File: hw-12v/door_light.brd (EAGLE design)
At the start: 26.2 x 28.6 mm, 24 parts, among them IC1 TINY13-20SSU, IC2 78L05F, T1 IRFML8244, T2 IRFML8244, T3 KP-3216P3C

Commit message: recalculated some resitors values
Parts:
- R2: value 470R -> 180R
- R7, R9: value 2.9kR -> 2.7kR
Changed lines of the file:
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@@
 <layer number="19" name="Unrouted" color="6" fill="1" visible="yes" active="yes"/>
 <layer number="20" name="Dimension" color="15" fill="1" visible="yes" active="yes"/>
-<layer number="21" name="tPlace" color="7" fill="1" visible="no" active="yes"/>
-<layer number="22" name="bPlace" color="7" fill="1" visible="no" active="yes"/>
-<layer number="23" name="tOrigins" color="15" fill="1" visible="no" active="yes"/>
-<layer number="24" name="bOrigins" color="15" fill="1" visible="no" active="yes"/>
+<layer number="21" name="tPlace" color="7" fill="1" visible="yes" active="yes"/>
+<layer number="22" name="bPlace" color="7" fill="1" visible="yes" active="yes"/>
+<layer number="23" name="tOrigins" color="15" fill="1" visible="yes" active="yes"/>
+<layer number="24" name="bOrigins" color="15" fill="1" visible="yes" active="yes"/>
 <layer number="25" name="tNames" color="7" fill="1" visible="no" active="yes"/>
 <layer number="26" name="bNames" color="7" fill="1" visible="no" active="yes"/>
@@
 <layer number="45" name="Holes" color="7" fill="1" visible="no" active="yes"/>
 <layer number="46" name="Milling" color="3" fill="1" visible="no" active="yes"/>
-<layer number="47" name="Measures" color="7" fill="1" visible="no" active="yes"/>
-<layer number="48" name="Document" color="7" fill="1" visible="no" active="yes"/>
-<layer number="49" name="Reference" color="7" fill="1" visible="no" active="yes"/>
-<layer number="51" name="tDocu" color="7" fill="1" visible="no" active="yes"/>
-<layer number="52" name="bDocu" color="7" fill="1" visible="no" active="yes"/>
+<layer number="47" name="Measures" color="7" fill="1" visible="yes" active="yes"/>
+<layer number="48" name="Document" color="7" fill="1" visible="yes" active="yes"/>
+<layer number="49" name="Reference" color="7" fill="1" visible="yes" active="yes"/>
+<layer number="51" name="tDocu" color="7" fill="1" visible="yes" active="yes"/>
+<layer number="52" name="bDocu" color="7" fill="1" visible="yes" active="yes"/>
 <layer number="91" name="Nets" color="2" fill="1" visible="no" active="no"/>
 <layer number="92" name="Busses" color="1" fill="1" visible="no" active="no"/>
@@
 <element name="F1" library="rcl" package="MINI_MELF-0204W" value="F750mA" x="47.41" y="50.47" rot="R90"/>
 <element name="R5" library="rcl" package="R0402" value="10kR" x="28.5" y="56"/>
-<element name="R7" library="rcl" package="R0603" value="2.9kR" x="33" y="45" rot="R180"/>
+<element name="R7" library="rcl" package="R0603" value="2.7kR" x="33" y="45" rot="R180"/>
 <element name="R8" library="rcl" package="R0603" value="10kR" x="26" y="56" rot="R90"/>
 <element name="R6" library="rcl" package="R0603" value="10kR" x="33" y="47"/>
-<element name="R9" library="rcl" package="R0603" value="2.9kR" x="26" y="47" rot="R90"/>
+<element name="R9" library="rcl" package="R0603" value="2.7kR" x="26" y="47" rot="R90"/>
 <element name="LED2" library="led" package="CHIPLED_1206" value="IR" x="42.28" y="45.55"/>
 <element name="LED1" library="led" package="CHIPLED_0603" value="RED" x="40" y="45"/>
-<element name="R2" library="rcl" package="R0603" value="470R" x="43" y="51" rot="R270"/>
+<element name="R2" library="rcl" package="R0603" value="180R" x="43" y="51" rot="R270"/>
 <element name="R1" library="rcl" package="R0603" value="470R" x="41" y="51" rot="R270"/>
 <element name="T3" library="opto-trans-smd" package="OPTO-TRANS-SIEMENS_BP103" value="KP-3216P3C" x="28.82" y="45.67" rot="R270">

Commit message: elements are now more compact
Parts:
- moved T3 3.68 mm to (32.5, 45.5), turned to 180 degrees
- moved R7 3.20 mm to (30.5, 47.0), turned to 0 degrees
- moved LED1 3.16 mm to (41.0, 48.0)
- moved LED2 2.83 mm to (39.5, 45.0), turned to 270 degrees
- moved R6 1.50 mm to (34.5, 47.0)
- moved SJ2 1.00 mm to (47.0, 45.0)
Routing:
- net N$1: track 4.81 -> 1.40 mm
- net N$2: track 3.15 -> 6.51 mm
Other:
- board size 26.2 x 28.6 mm -> 26.2 x 27.6 mm
- board text added: "v2.0.0 (rc7)"
- board text removed: "v2.0.0 (rc6)"
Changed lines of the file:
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@@
 <board>
 <plain>
-<wire x1="22.78" y1="40.75" x2="49" y2="40.75" width="0" layer="20"/>
-<wire x1="49" y1="40.75" x2="49" y2="69.38" width="0" layer="20"/>
+<wire x1="22.78" y1="41.75" x2="49" y2="41.75" width="0" layer="20"/>
+<wire x1="49" y1="41.75" x2="49" y2="69.38" width="0" layer="20"/>
 <wire x1="49" y1="69.38" x2="22.78" y2="69.38" width="0" layer="20"/>
-<wire x1="22.78" y1="69.38" x2="22.78" y2="40.75" width="0" layer="20"/>
-<text x="48.8" y="46.6" size="1.27" layer="1" rot="R90">+</text>
+<wire x1="22.78" y1="69.38" x2="22.78" y2="41.75" width="0" layer="20"/>
+<text x="48.8" y="47" size="1.27" layer="1" rot="R90">+</text>
 <text x="48.7" y="65.5" size="1.27" layer="1" rot="R90">LED</text>
 <text x="25.5" y="64.6" size="1.27" layer="1">v2.0.0
-(rc6)</text>
+(rc7)</text>
 </plain>
 <attributes>
@@
 <element name="F1" library="rcl" package="MINI_MELF-0204W" value="F750mA" x="47.41" y="50.47" rot="R90"/>
 <element name="R5" library="rcl" package="R0402" value="10kR" x="28.5" y="56"/>
-<element name="R7" library="rcl" package="R0603" value="2.7kR" x="33" y="45" rot="R180"/>
+<element name="R7" library="rcl" package="R0603" value="2.7kR" x="30.5" y="47"/>
 <element name="R8" library="rcl" package="R0603" value="10kR" x="26" y="56" rot="R90"/>
-<element name="R6" library="rcl" package="R0603" value="10kR" x="33" y="47"/>
+<element name="R6" library="rcl" package="R0603" value="10kR" x="34.5" y="47"/>
 <element name="R9" library="rcl" package="R0603" value="2.7kR" x="26" y="47" rot="R90"/>
-<element name="LED2" library="led" package="CHIPLED_1206" value="IR" x="42.28" y="45.55"/>
-<element name="LED1" library="led" package="CHIPLED_0603" value="RED" x="40" y="45"/>
+<element name="LED2" library="led" package="CHIPLED_1206" value="IR" x="39.5" y="45" rot="R270"/>
+<element name="LED1" library="led" package="CHIPLED_0603" value="RED" x="41" y="48"/>
 <element name="R2" library="rcl" package="R0603" value="180R" x="43" y="51" rot="R270"/>
 <element name="R1" library="rcl" package="R0603" value="470R" x="41" y="51" rot="R270"/>
-<element name="T3" library="opto-trans-smd" package="OPTO-TRANS-SIEMENS_BP103" value="KP-3216P3C" x="28.82" y="45.67" rot="R270">
-<attribute name="OC_NEWARK" value="unknown" x="28.82" y="45.67" size="1.778" layer="27" rot="R270" display="off"/>
-<attribute name="MPN" value="" x="28.82" y="45.67" size="1.778" layer="27" rot="R270" display="off"/>
-<attribute name="MF" value="" x="28.82" y="45.67" size="1.778" layer="27" rot="R270" display="off"/>
-<attribute name="OC_FARNELL" value="unknown" x="28.82" y="45.67" size="1.778" layer="27" rot="R270" display="off"/>
+<element name="T3" library="opto-trans-smd" package="OPTO-TRANS-SIEMENS_BP103" value="KP-3216P3C" x="32.5" y="45.5" rot="R180">
+<attribute name="OC_NEWARK" value="unknown" x="32.5" y="45.5" size="1.778" layer="27" rot="R180" display="off"/>
+<attribute name="MPN" value="" x="32.5" y="45.5" size="1.778" layer="27" rot="R180" display="off"/>
+<attribute name="MF" value="" x="32.5" y="45.5" size="1.778" layer="27" rot="R180" display="off"/>
+<attribute name="OC_FARNELL" value="unknown" x="32.5" y="45.5" size="1.778" layer="27" rot="R180" display="off"/>
 </element>
 <element name="T1" library="zetex" package="SOT-23" value="IRFML8244" x="38" y="51" rot="R180">
@@
 <attribute name="OC_FARNELL" value="unknown" x="38" y="51" size="1.778" layer="27" rot="R180" display="off"/>
 </element>
-<element name="SJ2" library="jumper" package="SJW" value="PWR" x="47" y="44" rot="R90"/>
+<element name="SJ2" library="jumper" package="SJW" value="PWR" x="47" y="45" rot="R90"/>
 <element name="SJ1" library="jumper" package="SJW" value="LIGHT" x="47.5" y="63.4" rot="R270"/>
 <element name="R4" library="rcl" package="R0603" value="100kR" x="32" y="63" rot="R180"/>
@@
 <contactref element="C1" pad="2"/>
 <polygon width="0.6096" layer="1" isolate="0.6096" orphans="yes">
-<vertex x="23.05" y="41.02"/>
+<vertex x="23.05" y="42.02"/>
 <vertex x="23.05" y="69.12"/>
 <vertex x="49.5" y="69.12"/>
-<vertex x="49.5" y="41.02"/>
+<vertex x="49.5" y="42.02"/>
 </polygon>
 <contactref element="R7" pad="1"/>
@@
 <contactref element="LED2" pad="C"/>
 <contactref element="R2" pad="2"/>
-<wire x1="43" y1="50.15" x2="43" y2="48.02" width="0.4064" layer="1"/>
-<wire x1="43" y1="48.02" x2="42.28" y2="47.3" width="0.4064" layer="1"/>
+<wire x1="41.25" y1="45" x2="41.72" y2="44.72" width="0.4064" layer="1"/>
+<wire x1="41.72" y1="44.72" x2="43" y2="46" width="0.4064" layer="1"/>
+<wire x1="43" y1="46" x2="43" y2="50.15" width="0.4064" layer="1"/>
 </signal>
 <signal name="N$4">
@@
 <contactref element="SJ2" pad="2"/>
 <wire x1="47.41" y1="48.97" x2="47.41" y2="45.68" width="0.8128" layer="1"/>
-<wire x1="47.41" y1="45.68" x2="47" y2="45.27" width="0.4064" layer="1"/>
+<wire x1="47.41" y1="45.68" x2="47" y2="46.27" width="0.4064" layer="1"/>
 </signal>
 <signal name="N$12">
@@
 <contactref element="IC1" pad="2"/>
 <contactref element="T3" pad="COLLECTOR"/>
-<wire x1="29.29" y1="47.04" x2="29.29" y2="47.29" width="0.4064" layer="1"/>
-<wire x1="29.29" y1="47.29" x2="30" y2="48" width="0.4064" layer="1"/>
-<wire x1="30" y1="48" x2="30" y2="52" width="0.4064" layer="1"/>
-<wire x1="32.15" y1="47" x2="32.15" y2="45" width="0.4064" layer="1"/>
 <wire x1="28.366" y1="52.635" x2="29.365" y2="52.635" width="0.4064" layer="1"/>
 <wire x1="29.365" y1="52.635" x2="30" y2="52" width="0.4064" layer="1"/>
-<wire x1="29.29" y1="47.04" x2="32.11" y2="47.04" width="0.4064" layer="1"/>
-<wire x1="32.11" y1="47.04" x2="32.15" y2="47" width="0.4064" layer="1"/>
+<wire x1="33.61" y1="47.04" x2="33.65" y2="47" width="0.4064" layer="1"/>
+<wire x1="30" y1="52" x2="30" y2="49" width="0.4064" layer="1"/>
+<wire x1="30" y1="49" x2="31.35" y2="47.65" width="0.4064" layer="1"/>
+<wire x1="31.35" y1="47" x2="31.35" y2="47.65" width="0.4064" layer="1"/>
+<wire x1="31.35" y1="47" x2="33.65" y2="47" width="0.4064" layer="1"/>
+<wire x1="33.65" y1="47" x2="33.65" y2="45.1" width="0.4064" layer="1"/>
+<wire x1="33.65" y1="45.1" x2="33.87" y2="45.03" width="0.4064" layer="1"/>
 </signal>
 <signal name="N$17">
@@
 <contactref element="LED1" pad="C"/>
 <contactref element="R1" pad="2"/>
-<wire x1="41" y1="50.15" x2="41" y2="49" width="0.4064" layer="1"/>
-<wire x1="41" y1="49" x2="40" y2="48" width="0.4064" layer="1"/>
-<wire x1="40" y1="48" x2="40" y2="45.75" width="0.4064" layer="1"/>
+<wire x1="41" y1="50.15" x2="41" y2="48.75" width="0.4064" layer="1"/>
 </signal>
 <signal name="N$14">
@@
 <wire x1="43" y1="57" x2="41.8" y2="57" width="0.4064" layer="1"/>
 <wire x1="41.8" y1="57" x2="41" y2="57.8" width="0.4064" layer="1"/>
-<wire x1="42.28" y1="43.8" x2="40.45" y2="43.8" width="0.4064" layer="1"/>
-<wire x1="40.45" y1="43.8" x2="40" y2="44.25" width="0.4064" layer="1"/>
-<wire x1="34" y1="47" x2="33.85" y2="47" width="0.4064" layer="1"/>
-<wire x1="37" y1="44" x2="39.75" y2="44" width="0.4064" layer="1"/>
-<wire x1="39.75" y1="44" x2="40" y2="44.25" width="0.4064" layer="1"/>
-<wire x1="34" y1="47" x2="37" y2="44" width="0.4064" layer="1"/>
-<wire x1="34" y1="47" x2="31" y2="50" width="0.4064" layer="1"/>
 <wire x1="31" y1="50" x2="31" y2="54.15" width="0.4064" layer="1"/>
 <wire x1="26.5" y1="59.5" x2="29.5" y2="59.5" width="0.4064" layer="1"/>
@@
 <wire x1="33.6" y1="58.4" x2="33" y2="59" width="0.4064" layer="1"/>
 <wire x1="33" y1="59" x2="30" y2="59" width="0.4064" layer="1"/>
+<wire x1="31" y1="50" x2="32" y2="49" width="0.4064" layer="1"/>
+<wire x1="32" y1="49" x2="34" y2="49" width="0.4064" layer="1"/>
+<wire x1="34" y1="49" x2="35.35" y2="47.65" width="0.4064" layer="1"/>
+<wire x1="35.35" y1="47" x2="35.35" y2="47.65" width="0.4064" layer="1"/>
+<wire x1="35.35" y1="47" x2="36" y2="47" width="0.4064" layer="1"/>
+<wire x1="36" y1="47" x2="38" y2="45" width="0.4064" layer="1"/>
+<wire x1="38" y1="45" x2="38" y2="44.92" width="0.4064" layer="1"/>
+<wire x1="38" y1="44.92" x2="37.75" y2="45" width="0.4064" layer="1"/>
+<wire x1="38" y1="45" x2="40" y2="47" width="0.4064" layer="1"/>
+<wire x1="40" y1="47" x2="40.75" y2="47" width="0.4064" layer="1"/>
+<wire x1="40.75" y1="47" x2="41" y2="47.25" width="0.4064" layer="1"/>
 </signal>
 <signal name="+12V">

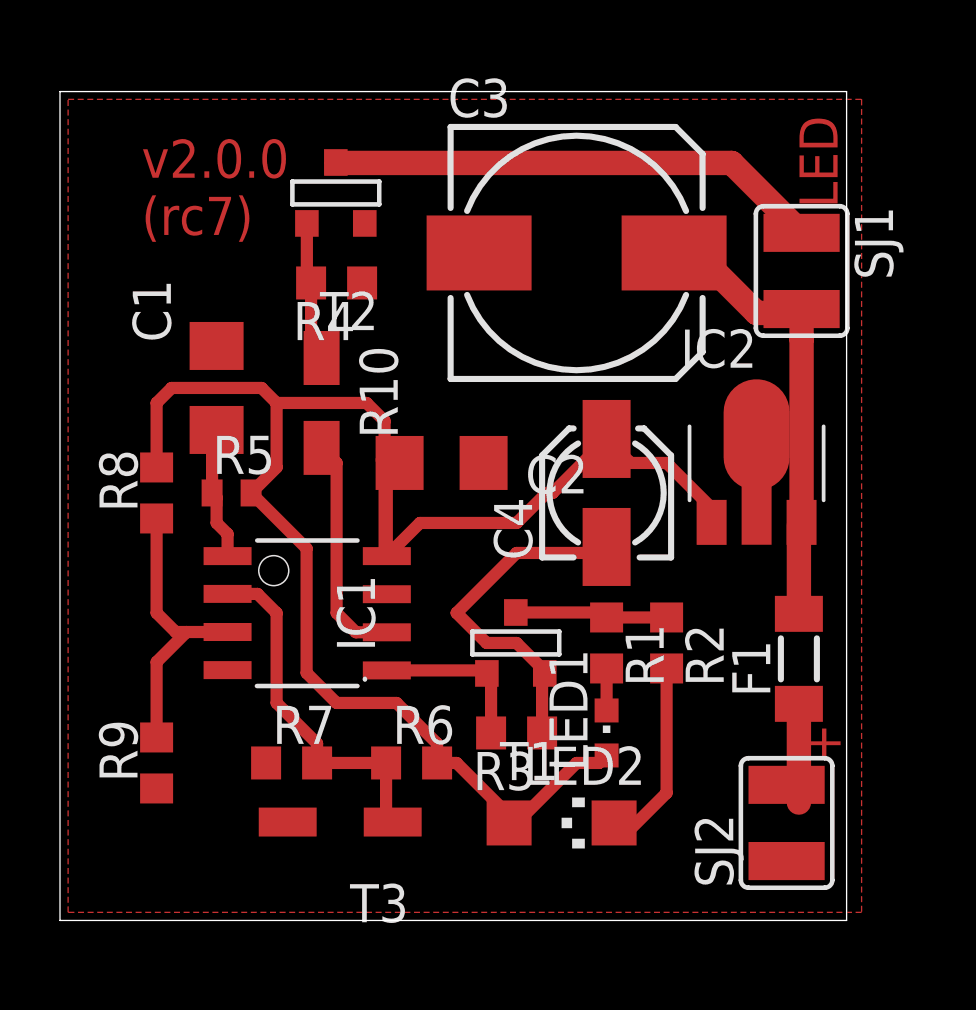
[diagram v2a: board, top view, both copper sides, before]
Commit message: fixed coliding Vcc and GND on board layout
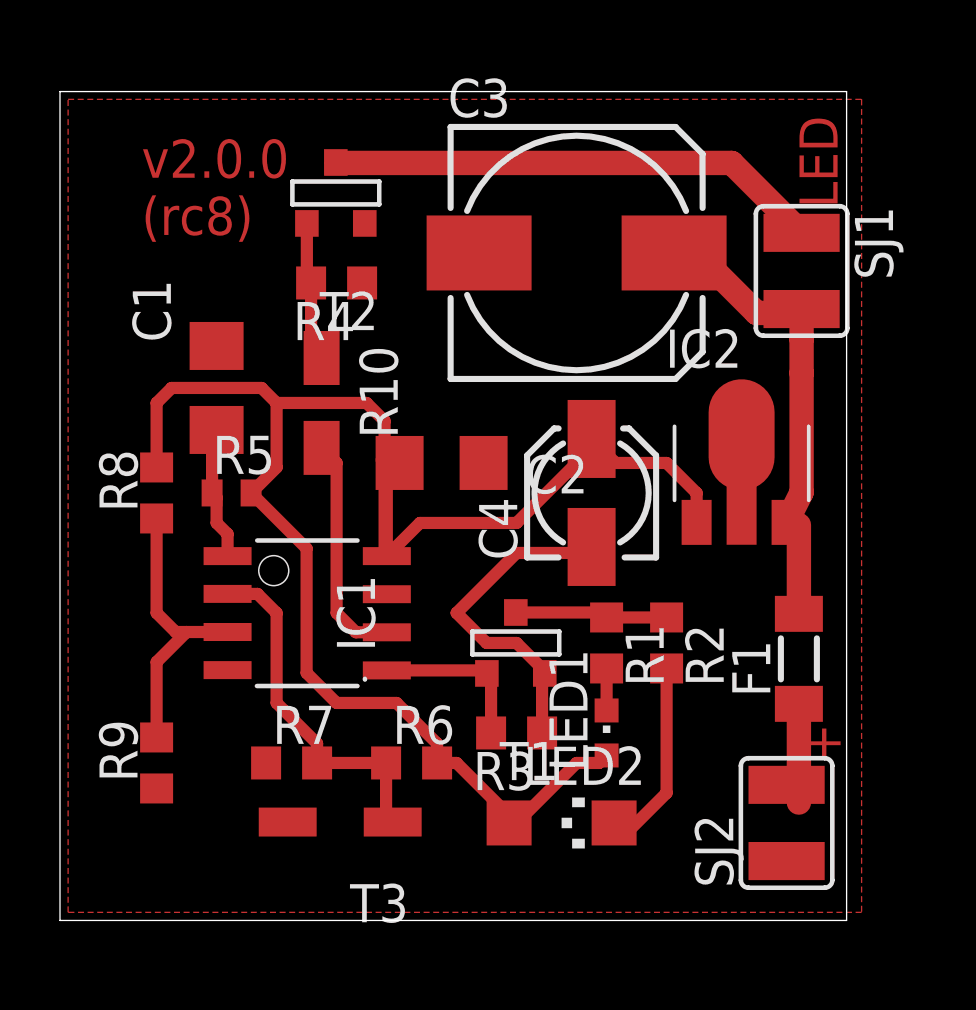
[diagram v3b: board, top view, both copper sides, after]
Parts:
- moved C4 0.50 mm to (40.5, 56.0)
- moved IC2 0.50 mm to (45.5, 57.0)
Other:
- board text added: "v2.0.0 (rc8)"
- board text removed: "v2.0.0 (rc7)"
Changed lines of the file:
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@@
 <text x="48.7" y="65.5" size="1.27" layer="1" rot="R90">LED</text>
 <text x="25.5" y="64.6" size="1.27" layer="1">v2.0.0
-(rc7)</text>
+(rc8)</text>
 </plain>
 <attributes>
@@
 <attribute name="OC_FARNELL" value="unknown" x="32" y="66" size="1.778" layer="27" rot="R180" display="off"/>
 </element>
-<element name="C4" library="rcl" package="153CLV-0405" value="4.7uF" x="41" y="56" rot="R90"/>
+<element name="C4" library="rcl" package="153CLV-0405" value="4.7uF" x="40.5" y="56" rot="R90"/>
 <element name="C3" library="rcl" package="153CLV-0810" value="100uF" x="40" y="64"/>
-<element name="IC2" library="linear" package="SOT89" value="78L05F" x="46" y="57"/>
+<element name="IC2" library="linear" package="SOT89" value="78L05F" x="45.5" y="57"/>
 <element name="R10" library="rcl" package="R1206W" value="0R" x="31.5" y="59" rot="R270"/>
 </elements>
@@
 <wire x1="36" y1="52" x2="38" y2="54" width="0.4064" layer="1"/>
 <wire x1="38" y1="54" x2="40.8" y2="54" width="0.4064" layer="1"/>
-<wire x1="40.8" y1="54" x2="41" y2="54.2" width="0.4064" layer="1"/>
+<wire x1="40.8" y1="54" x2="40.5" y2="54.2" width="0.4064" layer="1"/>
 </signal>
 <signal name="N$2">
@@
 <contactref element="IC2" pad="1"/>
 <contactref element="C4" pad="+"/>
-<wire x1="44.501" y1="55.019" x2="44.501" y2="55.499" width="0.4064" layer="1"/>
-<wire x1="44.501" y1="55.499" x2="43" y2="57" width="0.4064" layer="1"/>
-<wire x1="43" y1="57" x2="41.8" y2="57" width="0.4064" layer="1"/>
-<wire x1="41.8" y1="57" x2="41" y2="57.8" width="0.4064" layer="1"/>
 <wire x1="31" y1="50" x2="31" y2="54.15" width="0.4064" layer="1"/>
 <wire x1="26.5" y1="59.5" x2="29.5" y2="59.5" width="0.4064" layer="1"/>
@@
 <wire x1="34.1" y1="57" x2="33.6" y2="56.4" width="0.4064" layer="1"/>
 <wire x1="34.779" y1="55" x2="38" y2="55" width="0.4064" layer="1"/>
-<wire x1="38" y1="55" x2="39" y2="56" width="0.4064" layer="1"/>
-<wire x1="39" y1="56" x2="39.2" y2="56" width="0.4064" layer="1"/>
 <wire x1="31" y1="54.15" x2="29.15" y2="56" width="0.4064" layer="1"/>
-<wire x1="39.2" y1="56" x2="41" y2="57.8" width="0.4064" layer="1"/>
 <wire x1="33.674" y1="53.895" x2="33.674" y2="56.326" width="0.4064" layer="1"/>
 <wire x1="33.674" y1="56.326" x2="33.6" y2="56.4" width="0.4064" layer="1"/>
@@
 <wire x1="40" y1="47" x2="40.75" y2="47" width="0.4064" layer="1"/>
 <wire x1="40.75" y1="47" x2="41" y2="47.25" width="0.4064" layer="1"/>
+<wire x1="40.5" y1="57.8" x2="40.5" y2="57.5" width="0.4064" layer="1"/>
+<wire x1="40.5" y1="57.5" x2="38" y2="55" width="0.4064" layer="1"/>
+<wire x1="44.001" y1="55.019" x2="44.001" y2="55.999" width="0.4064" layer="1"/>
+<wire x1="44.001" y1="55.999" x2="43" y2="57" width="0.4064" layer="1"/>
+<wire x1="43" y1="57" x2="41.3" y2="57" width="0.4064" layer="1"/>
+<wire x1="41.3" y1="57" x2="40.5" y2="57.8" width="0.4064" layer="1"/>
 </signal>
 <signal name="+12V">
@@
 <contactref element="C3" pad="+"/>
 <wire x1="47.41" y1="51.97" x2="47.41" y2="54.93" width="0.8128" layer="1"/>
-<wire x1="47.41" y1="54.93" x2="47.499" y2="55.019" width="0.4064" layer="1"/>
-<wire x1="47.499" y1="55.019" x2="47.499" y2="61.131" width="0.8128" layer="1"/>
+<wire x1="47.41" y1="54.93" x2="46.999" y2="55.019" width="0.4064" layer="1"/>
+<wire x1="46.999" y1="55.019" x2="47.5" y2="56.02" width="0.8128" layer="1"/>
+<wire x1="47.5" y1="56.02" x2="47.5" y2="60" width="0.8128" layer="1"/>
+<wire x1="47.5" y1="60" x2="47.499" y2="61.131" width="0.8128" layer="1"/>
 <wire x1="47.499" y1="61.131" x2="47.5" y2="62.13" width="0.8128" layer="1"/>
 <wire x1="43.25" y1="64" x2="44" y2="64" width="0.4064" layer="1"/>
